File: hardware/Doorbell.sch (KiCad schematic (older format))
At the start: 21 parts, among them CON1 +5Vdc unreg 2.5mm, P1 SENSE, P2 ESP8266, SW1 RESET, U1 HP4510, U2 LM3940

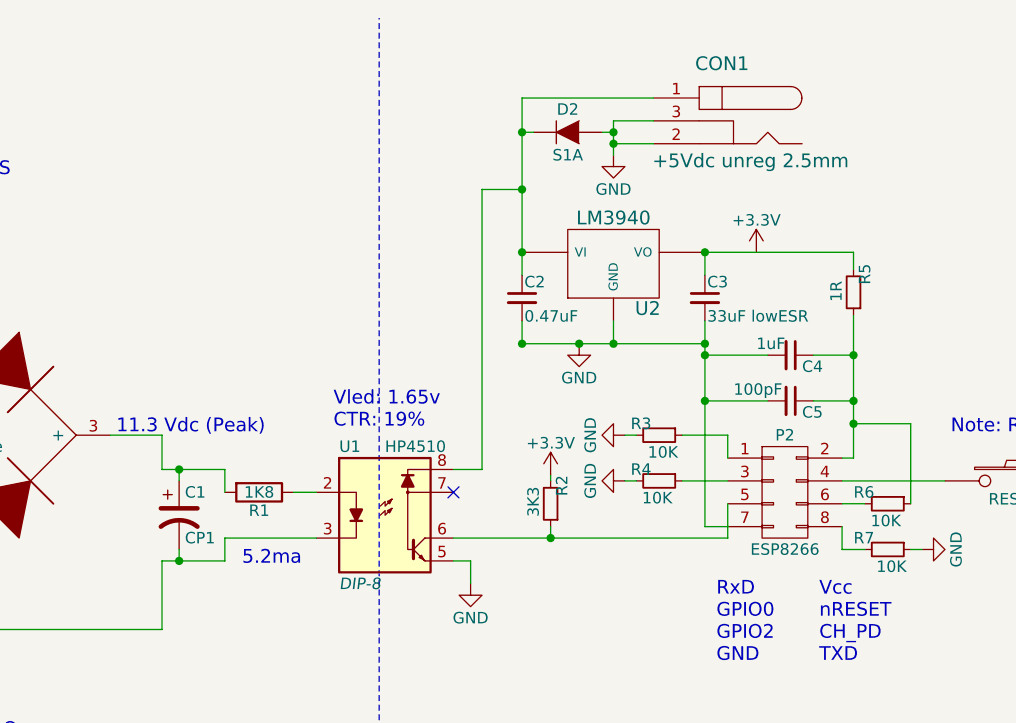
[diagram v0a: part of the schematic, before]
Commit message: Added a missing junction (3v3 power net to output of regulator)
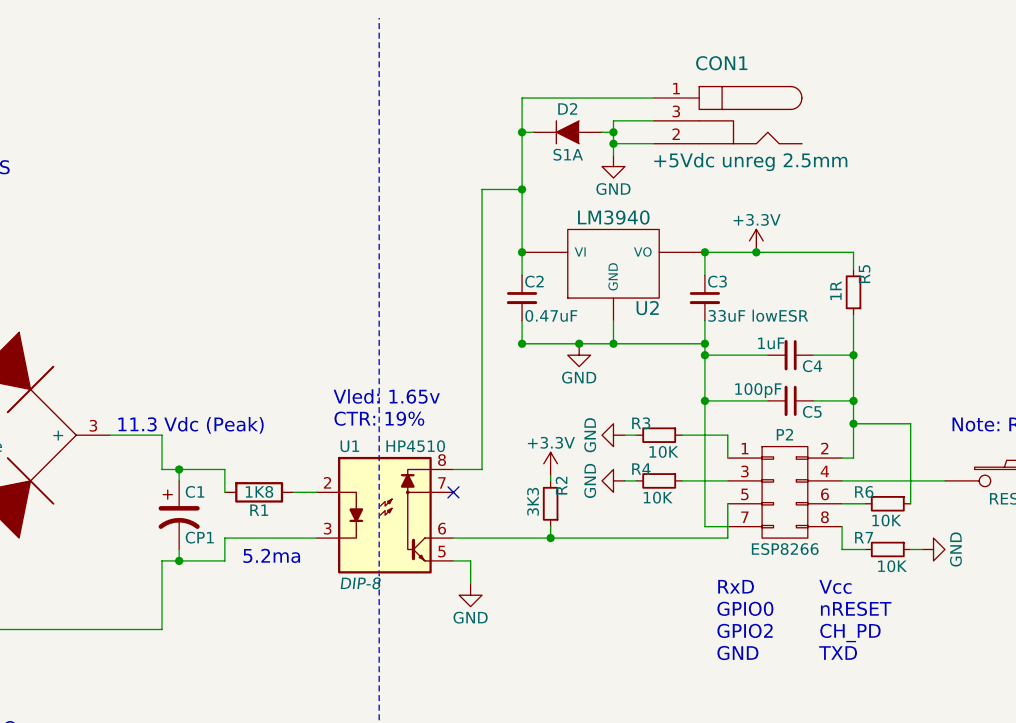
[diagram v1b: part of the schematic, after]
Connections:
- net +3V3: now also C3.1, R5.2, U2.VO
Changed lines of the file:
@@
 	2900 2550 3000 2550
 Wire Wire Line
-	2325 2450 2600 2450
+	2325 2450 2400 2450
+Wire Wire Line
+	2400 2450 2600 2450
 Wire Wire Line
 	2600 2450 2600 2550
@@
 	2600 2750 2600 2850
 Wire Wire Line
-	2600 2850 2325 2850
+	2600 2850 2400 2850
+Wire Wire Line
+	2400 2850 2325 2850
 Connection ~ 2400 2450
 Connection ~ 2400 2850
@@
 	4700 1500 4700 1600
 Wire Wire Line
-	3900 825  3900 1600
+	3900 825  3900 975
+Wire Wire Line
+	3900 975  3900 1225
+Wire Wire Line
+	3900 1225 3900 1500
+Wire Wire Line
+	3900 1500 3900 1600
 Wire Wire Line
 	3900 1800 3900 1900
 Wire Wire Line
-	4700 1800 4700 2700
+	4700 1800 4700 1900
 Wire Wire Line
-	4700 1500 5350 1500
+	4700 1900 4700 1950
+Wire Wire Line
+	4700 1950 4700 2150
+Wire Wire Line
+	4700 2150 4700 2700
+Wire Wire Line
+	4700 1500 4925 1500
+Wire Wire Line
+	4925 1500 5350 1500
 Connection ~ 4700 1500
 Wire Wire Line
@@
 	4475 925  4300 925
 Wire Wire Line
-	4300 925  4300 1075
+	4300 925  4300 975
+Wire Wire Line
+	4300 975  4300 1025
+Wire Wire Line
+	4300 1025 4300 1075
 Wire Wire Line
 	4475 1025 4300 1025
@@
 	4800 2750 4800 2600
 Wire Wire Line
-	3600 2750 4800 2750
+	3600 2750 4025 2750
+Wire Wire Line
+	4025 2750 4800 2750
 Wire Wire Line
 	4025 2475 4025 2500
@@
 	5350 1500 5350 1575
 Wire Wire Line
-	5350 1775 5350 2400
+	5350 1775 5350 1950
 Wire Wire Line
-	3900 1900 4700 1900
+	5350 1950 5350 2150
+Wire Wire Line
+	5350 2150 5350 2250
+Wire Wire Line
+	5350 2250 5350 2400
+Wire Wire Line
+	3900 1900 4150 1900
+Wire Wire Line
+	4150 1900 4300 1900
+Wire Wire Line
+	4300 1900 4700 1900
 $Comp
 L D D2
@@
 	3950 975  3900 975
 Connection ~ 3900 975
+Connection ~ 4925 1500
 $EndSCHEMATC

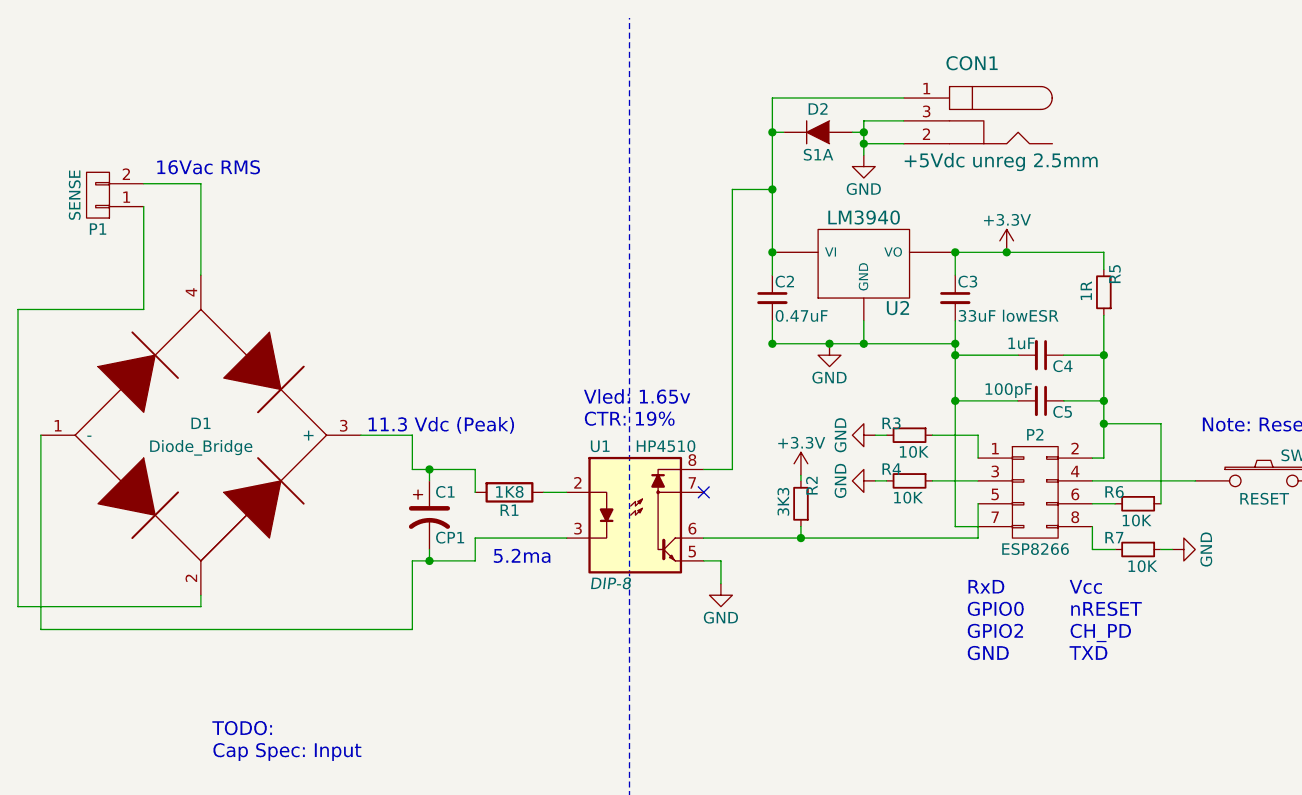
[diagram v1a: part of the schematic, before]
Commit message: More work on schematic, initial layout. need to make a footprint for the vreg and the anti-stupid diode
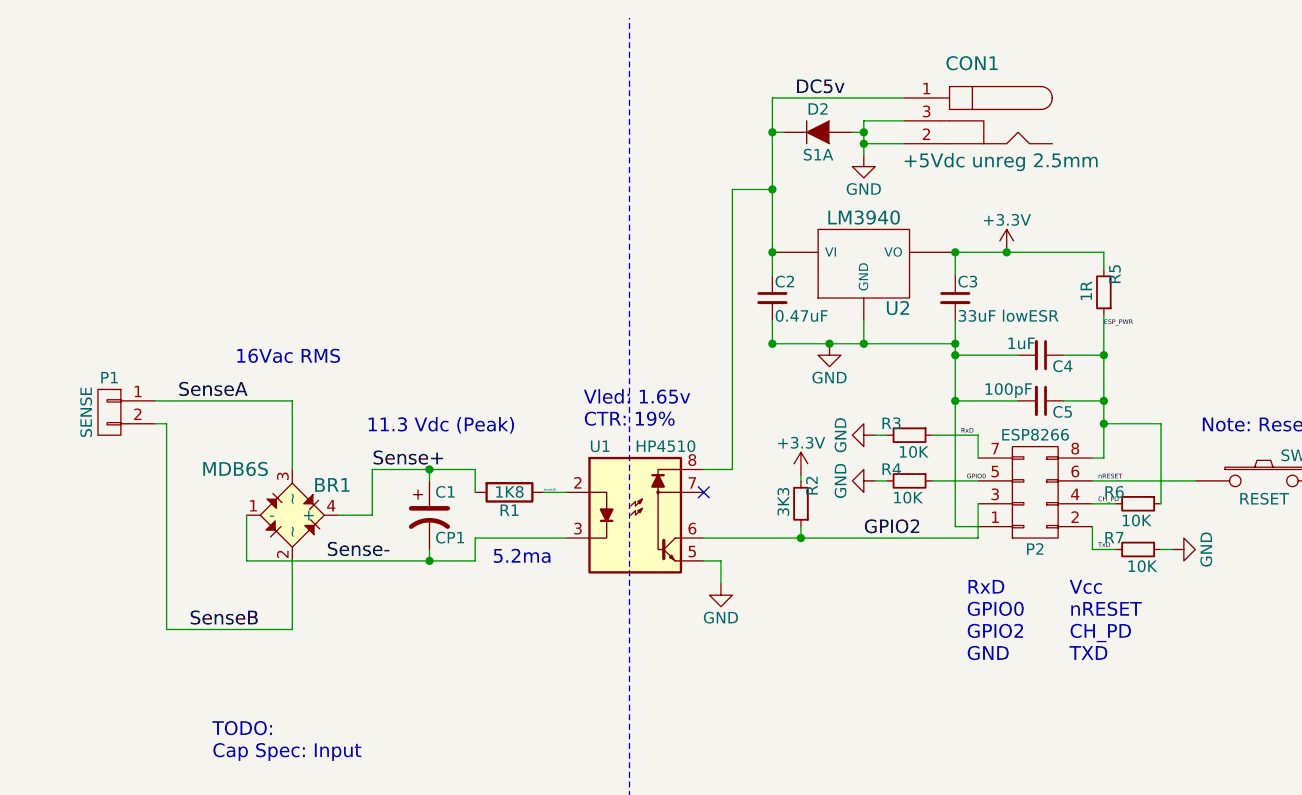
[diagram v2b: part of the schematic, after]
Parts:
- removed D1: Diode_Bridge, symbol Diode_Bridge
- added BR1: MDB6S, footprints:Micro-DIP, symbol DiodeBridge
- C1: footprint (none) -> Capacitors_ThroughHole:C_Radial_D14_L25_P5
- C2, C4, C5: footprint (none) -> Capacitors_SMD:C_0603_HandSoldering
- C3: footprint (none) -> Capacitors_ThroughHole:C_Radial_D8_L11.5_P3.5; Part No (none) -> RNU1J330MDN1KX
- CON1: footprint (none) -> Connect:BARREL_JACK
- D2: footprint (none) -> Diodes_SMD:DO-214AB_Handsoldering
- P1: footprint (none) -> Pin_Headers:Pin_Header_Angled_1x02
- P2: footprint (none) -> Socket_Strips:Socket_Strip_Straight_2x04
- R1, R2, R3, R4, R5, R6, R7, R8: footprint (none) -> Resistors_SMD:R_0603_HandSoldering
- SW1: footprint (none) -> Buttons_Switches_SMD:SW_SPST_B3S-1000
- U1: footprint DIP-8 -> Housings_DIP:DIP-8_W7.62mm
- U2: footprint (none) -> Power_Integrations:TO-220
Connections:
- net GND: now also P2.1 (P1); no longer P2.7 (P7)
- net SenseLED: now reaches R1.1, U1.2
- net Sense-: now reaches C1.2, U1.3
- net Sense-: now also BR1.1 (-)
- net GPIO2: now reaches R2.1, U1.6
- net GPIO2: now also P2.3 (P3); no longer P2.5 (P5)
- net DC5v: now reaches C2.1, CON1.1, D2.1 (K), U1.8, U2.VI
- net SenseA: now reaches P1.1 (P1)
- net SenseA: now also BR1.3 (~~)
- net Sense+: now reaches C1.1, R1.2
- net Sense+: now also BR1.4 (+)
- net SenseB: now reaches P1.2 (P2)
- net SenseB: now also BR1.2 (~~)
- net RxD: now reaches R3.1
- net RxD: now also P2.7 (P7); no longer P2.1 (P1)
- net ESP_PWR: now reaches C4.1, C5.1, R5.1, R6.1
- net ESP_PWR: now also P2.8 (P8); no longer P2.2 (P2)
- net GPIO0: now reaches R4.1
- net GPIO0: now also P2.5 (P5); no longer P2.3 (P3)
- net CH_PD: now reaches P2.4 (P4)
- net CH_PD: now also R6.2; no longer SW1.1
- net nRESET: now reaches P2.6 (P6)
- net nRESET: now also SW1.1; no longer R6.2
- net TxD: now reaches R7.2
- net TxD: now also P2.2 (P2); no longer P2.8 (P8)
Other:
- moved on the sheet: P1
